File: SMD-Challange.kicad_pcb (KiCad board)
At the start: 2 copper layers, 40 x 40 mm, 20 parts, among them SW1 SW_DPDT_x2, U1 NE555, U2 4017

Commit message: finish design of nibble++ :)
Signed-off-by: Thomas Schmid <tom@binary-kitchen.de>
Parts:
- added G***: Nibble++, SMD-Challange:Nibble++, F.Cu at (96.6, 97.3)
- added G***: kitchen_head, SMD-Challange:kitchen_head, F.Cu at (92.6, 89.8)
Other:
- board text added: "Nibble++"
- board text added: "V1.0"

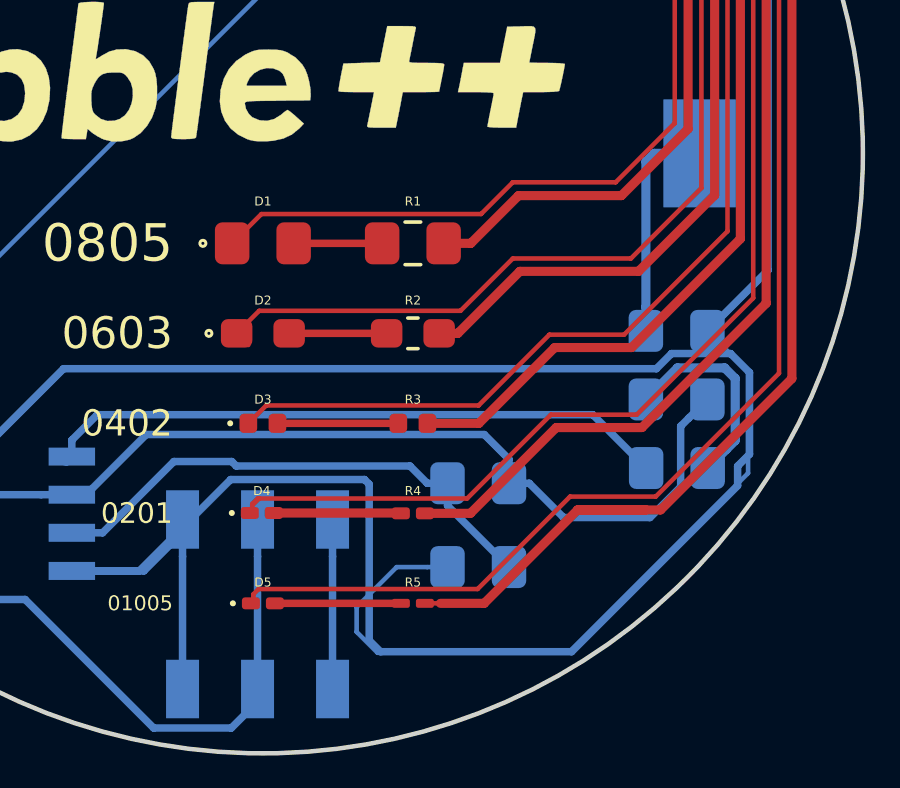
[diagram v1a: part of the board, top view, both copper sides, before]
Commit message: Changed track-layout slightly for better soldering
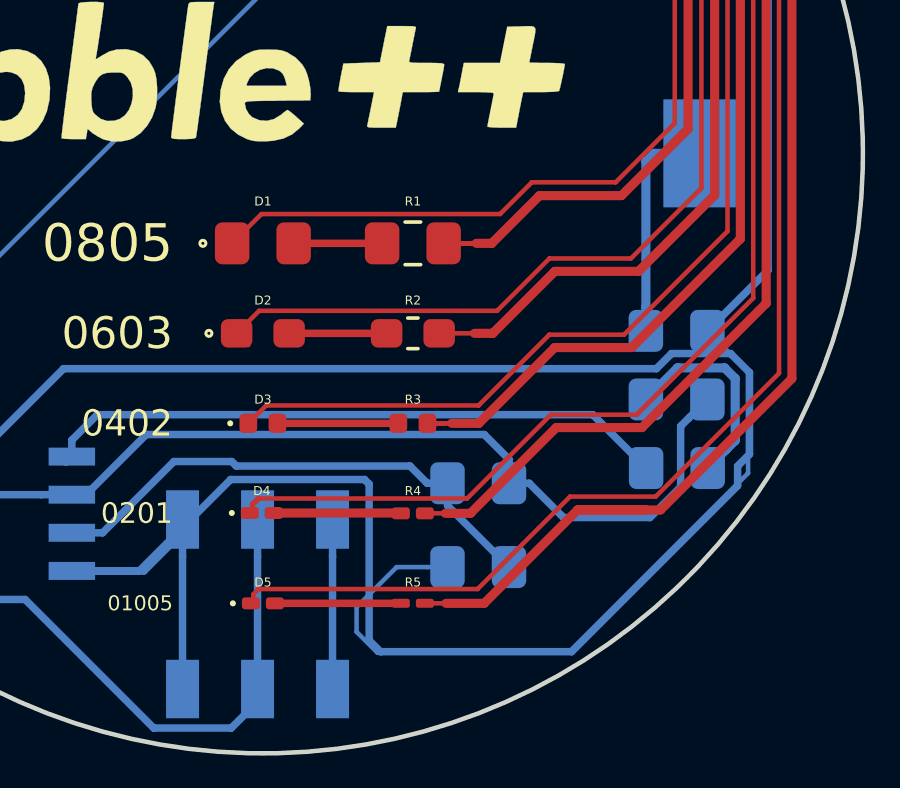
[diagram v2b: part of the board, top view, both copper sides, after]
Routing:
- net Net-(R1-Pad2): track 25.7 -> 26.6 mm
- net Net-(R3-Pad2): track 37.0 -> 37.6 mm
